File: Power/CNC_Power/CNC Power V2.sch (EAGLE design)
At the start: 73 parts, among them Q1 BC807-40LT1SMD, Q2 BC817-40LT1SMD, Q3 IRF740, Q4 IRF740, Q5 STD6NF10, U1 SG3525AN, X1 MKDSN1,5/2-5,08, X2 MKDSN1,5/2-5,08, X3 MKDSN1,5/2-5,08

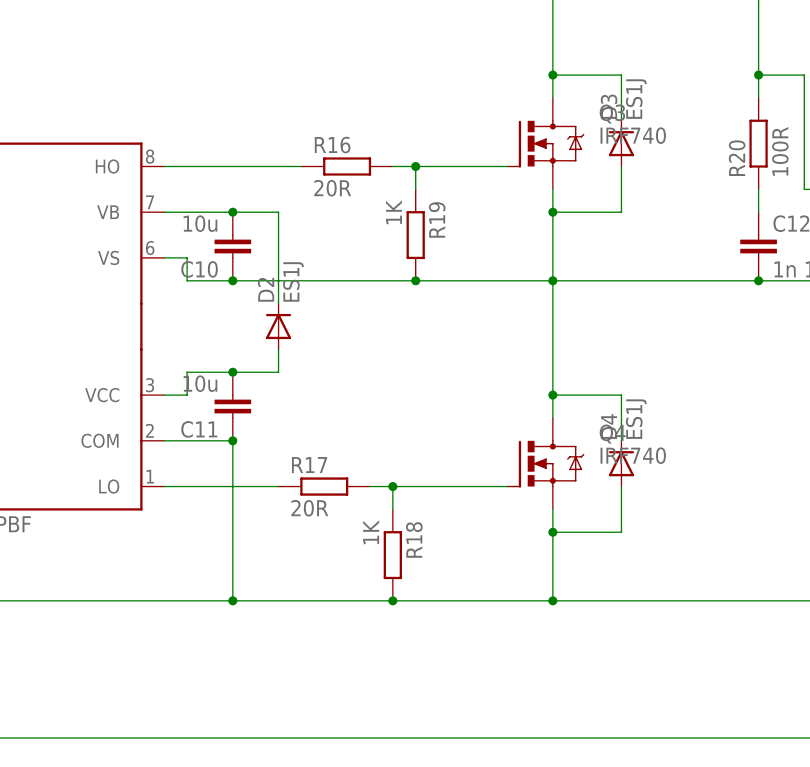
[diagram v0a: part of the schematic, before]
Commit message: Изменения в обратной связи схеме драйвера
Резисторы в базах мосфетов заменены на выводные, изменена разводка
обратной связи в районе TL431
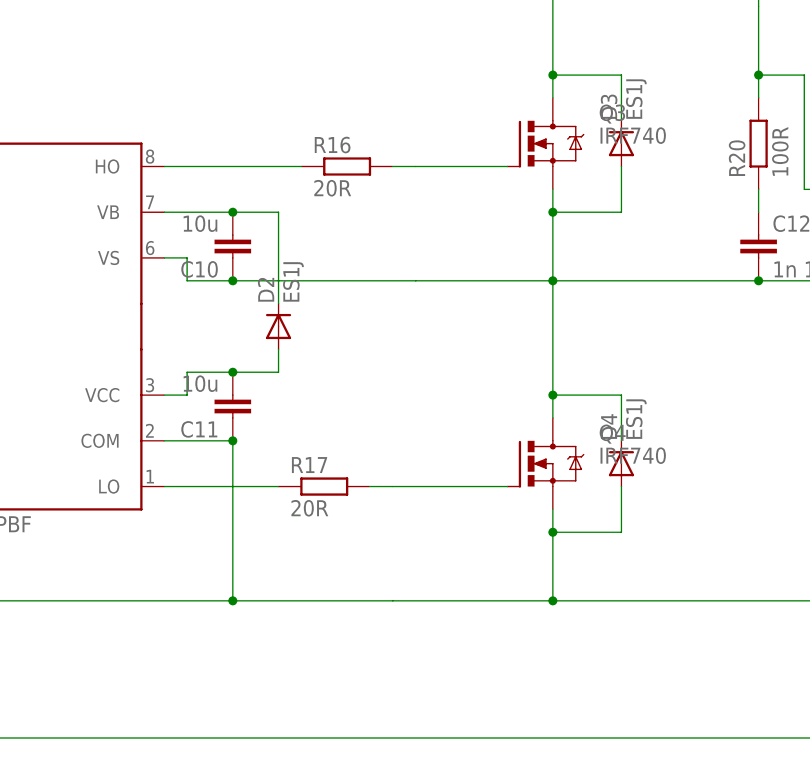
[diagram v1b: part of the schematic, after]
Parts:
- removed R18, R19: 1K, rcl:R-EU_R0805
- R16, R17: device rcl:R-EU_R1206 -> rcl:R-EU_0309/12
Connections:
- net HV-0: no longer R18.2
- net N$17: no longer R18.1
- net N$7: no longer R19.1
- net VS: no longer R19.2

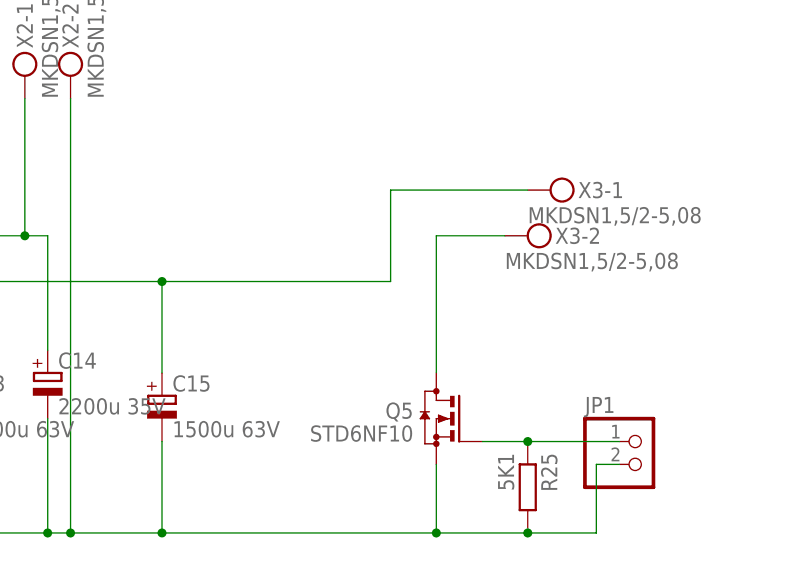
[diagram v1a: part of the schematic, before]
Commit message: Добавил диод параллельно двигателю
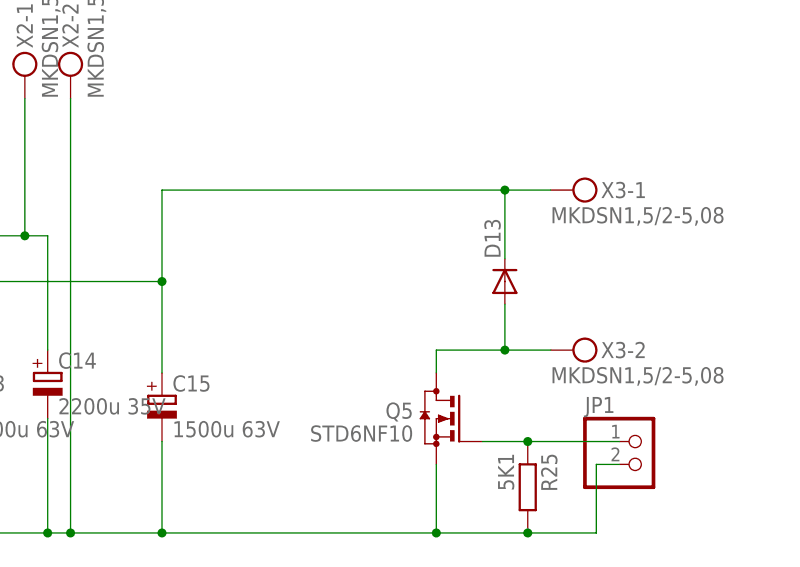
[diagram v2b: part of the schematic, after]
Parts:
- added D13: (no value), diode:DIODE-DO220S
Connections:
- net N$36: now also D13.C
- net N$45: now also D13.A
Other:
- moved on the sheet: X3-1, X3-2
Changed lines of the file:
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@@
 <part name="JP2" library="pinhead" deviceset="PINHD-1X2" device=""/>
 <part name="R26" library="rcl" deviceset="R-EU_" device="0207/10" value="160k"/>
+<part name="D13" library="diode" deviceset="DIODE-" device="DO220S"/>
 </parts>
 <sheets>
@@
 <instance part="X2" gate="-1" x="271.78" y="-45.72" rot="R90"/>
 <instance part="X2" gate="-2" x="276.86" y="-45.72" rot="R90"/>
-<instance part="X3" gate="-1" x="330.2" y="-58.42"/>
-<instance part="X3" gate="-2" x="327.66" y="-63.5"/>
+<instance part="X3" gate="-1" x="332.74" y="-58.42"/>
+<instance part="X3" gate="-2" x="332.74" y="-76.2"/>
 <instance part="JP1" gate="G$1" x="340.36" y="-88.9"/>
 <instance part="R25" gate="G$1" x="327.66" y="-91.44" rot="R270"/>
 <instance part="JP2" gate="G$1" x="185.42" y="-25.4" rot="MR90"/>
 <instance part="R26" gate="G$1" x="27.94" y="27.94" rot="R90"/>
+<instance part="D13" gate="G$1" x="325.12" y="-68.58" rot="R90"/>
 </instances>
 <busses>
@@
 <junction x="259.08" y="-101.6"/>
 <pinref part="X3" gate="-1" pin="KL"/>
-<wire x1="327.66" y1="-58.42" x2="312.42" y2="-58.42" width="0.1524" layer="91"/>
-<wire x1="312.42" y1="-58.42" x2="312.42" y2="-68.58" width="0.1524" layer="91"/>
-<wire x1="312.42" y1="-68.58" x2="287.02" y2="-68.58" width="0.1524" layer="91"/>
+<wire x1="330.2" y1="-58.42" x2="325.12" y2="-58.42" width="0.1524" layer="91"/>
+<wire x1="325.12" y1="-58.42" x2="287.02" y2="-58.42" width="0.1524" layer="91"/>
+<wire x1="287.02" y1="-58.42" x2="287.02" y2="-68.58" width="0.1524" layer="91"/>
 <junction x="287.02" y="-68.58"/>
+<pinref part="D13" gate="G$1" pin="C"/>
+<wire x1="325.12" y1="-66.04" x2="325.12" y2="-58.42" width="0.1524" layer="91"/>
+<junction x="325.12" y="-58.42"/>
 </segment>
 </net>
@@
 <pinref part="X3" gate="-2" pin="KL"/>
 <pinref part="Q5" gate="G$1" pin="D"/>
-<wire x1="325.12" y1="-63.5" x2="317.5" y2="-63.5" width="0.1524" layer="91"/>
-<wire x1="317.5" y1="-63.5" x2="317.5" y2="-78.74" width="0.1524" layer="91"/>
-</segment>
-</net>
+<wire x1="330.2" y1="-76.2" x2="325.12" y2="-76.2" width="0.1524" layer="91"/>
+<wire x1="325.12" y1="-76.2" x2="317.5" y2="-76.2" width="0.1524" layer="91"/>
+<wire x1="317.5" y1="-76.2" x2="317.5" y2="-78.74" width="0.1524" layer="91"/>
+<pinref part="D13" gate="G$1" pin="A"/>
+<wire x1="325.12" y1="-71.12" x2="325.12" y2="-76.2" width="0.1524" layer="91"/>
+<junction x="325.12" y="-76.2"/>
+</segment>
+</net>
